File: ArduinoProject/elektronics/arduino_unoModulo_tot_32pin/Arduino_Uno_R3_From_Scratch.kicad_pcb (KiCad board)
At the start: 2 copper layers, 56.9 x 47.8 mm, 35 parts, among them IC401 MC33269ST-5.OT3, J201 POWER, J202 IOL, J203 IOL, J204 IOL, SW601 RESET_SWITCH, U301 74AHC1G04, U302 L298D, U303 74AHC1G04, U402 LP2985-3.3, U601 ATMEGA328P-MU20, X1 DG3XX-04-3.5, X2 DG3XX-02-3.5, X601 CSTCE16MOV53-R0

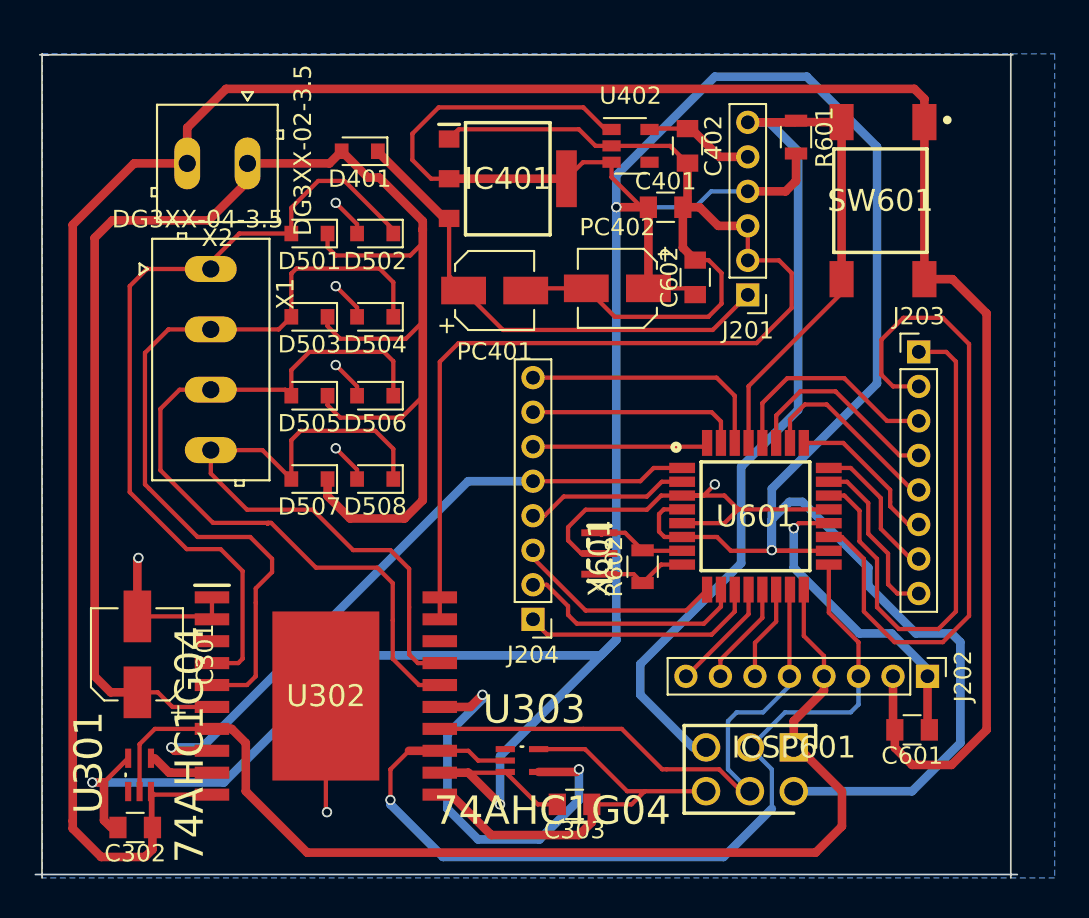
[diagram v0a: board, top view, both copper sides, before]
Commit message: arduino footprint altered
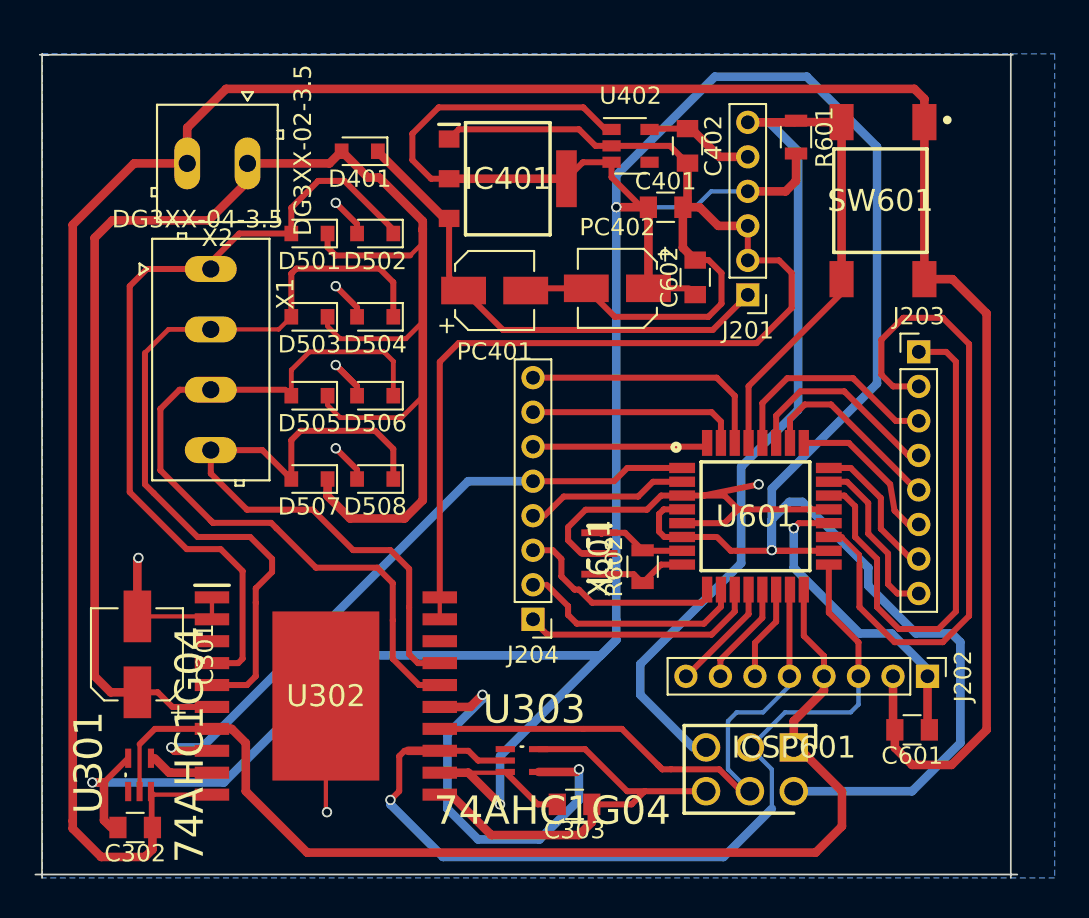
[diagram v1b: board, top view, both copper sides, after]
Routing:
- net GND: track 315.3 -> 319.4 mm
- net /ATMEGA328P/AD6: track 39.5 -> 42.1 mm
- net /ATMEGA328P/IO5: track 12.3 -> 13.0 mm
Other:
- net class Default: trace_width 0.25 -> 0.35

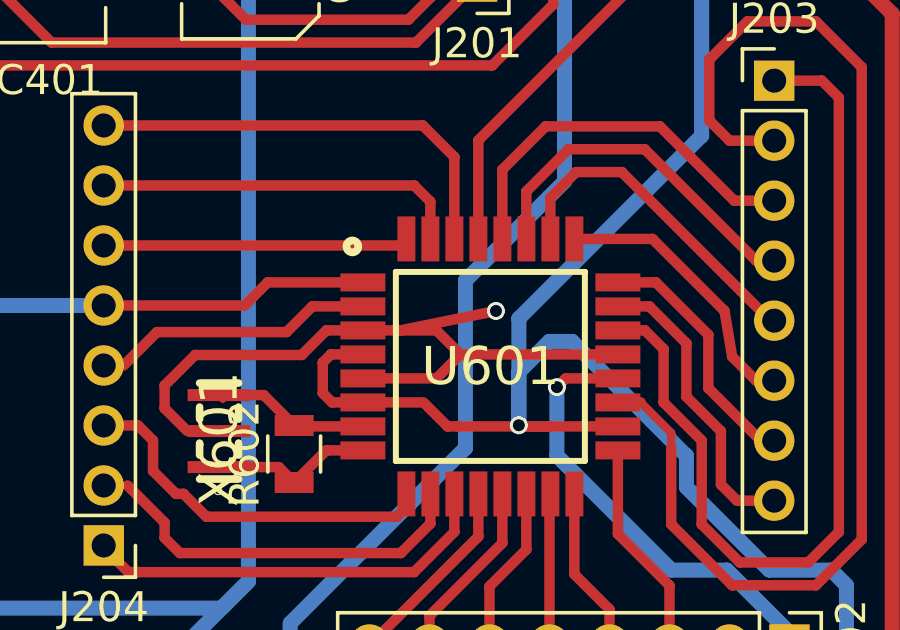
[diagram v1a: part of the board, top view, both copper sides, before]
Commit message: arduino footprint altered2
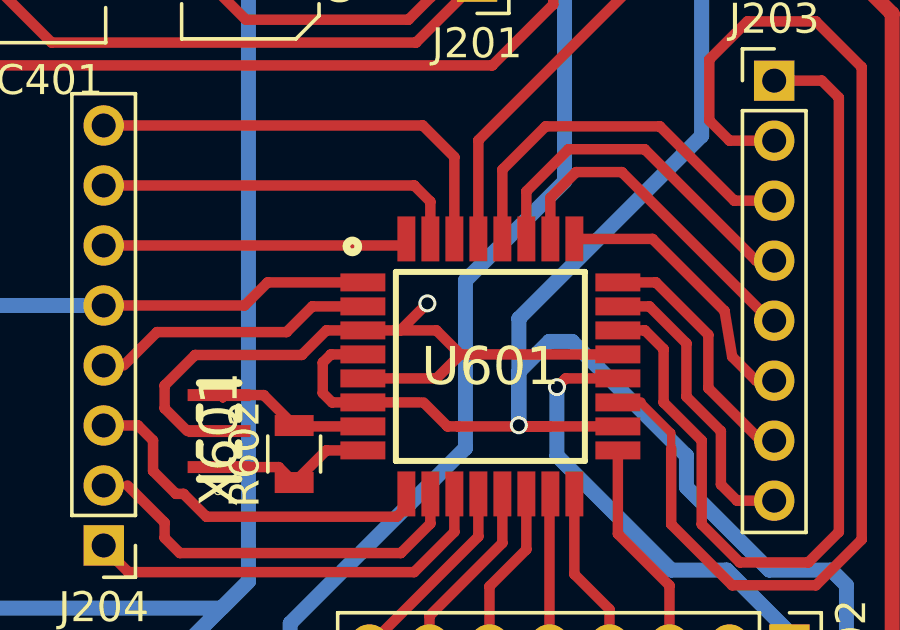
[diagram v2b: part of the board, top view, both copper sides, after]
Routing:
- net GND: track 319.4 -> 317.4 mm
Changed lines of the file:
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@@
   (general
     (links 119)
-    (no_connects 1)
+    (no_connects 0)
     (area 146.185999 91.125523 205.296001 140.678)
     (thickness 1.6)
@@
   (layers
     (0 F.Cu signal)
-    (31 B.Cu signal hide)
+    (31 B.Cu signal)
     (32 B.Adhes user)
     (33 F.Adhes user)
@@
     (pad_drill 0.6)
     (pad_to_mask_clearance 0)
-    (aux_axis_origin 0 0)
+    (aux_axis_origin 236.152 136.455)
     (grid_origin 166.81 124.771)
     (visible_elements FFFFFF5F)
@@
   (segment (start 199.37 105.515) (end 197.749 105.515) (width 0.5) (layer F.Cu) (net 2))
   (segment (start 183.71 118.053) (end 184.958 118.053) (width 0.25) (layer F.Cu) (net 2))
-  (via (at 188.146 117.405) (size 0.6) (drill 0.4) (layers F.Cu B.Cu) (net 2))
-  (segment (start 184.958 118.053) (end 188.146 117.405) (width 0.35) (layer F.Cu) (net 2))
+  (via (at 185.86 117.151) (size 0.6) (drill 0.4) (layers F.Cu B.Cu) (net 2))
+  (segment (start 184.958 118.053) (end 185.86 117.151) (width 0.35) (layer F.Cu) (net 2))
   (segment (start 195.93 128.524) (end 195.93 131.523) (width 0.5) (layer F.Cu) (net 2))
   (segment (start 195.93 131.523) (end 196.036 131.629) (width 0.25) (layer F.Cu) (net 2))
